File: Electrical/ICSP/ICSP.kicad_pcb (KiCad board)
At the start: 2 copper layers, 8 parts, among them J1 card_edge_6p, J2 card_edge_6p, J3 card_edge_6p, J4 card_edge_6p, J5 card_edge_6p, J6 card_edge_6p

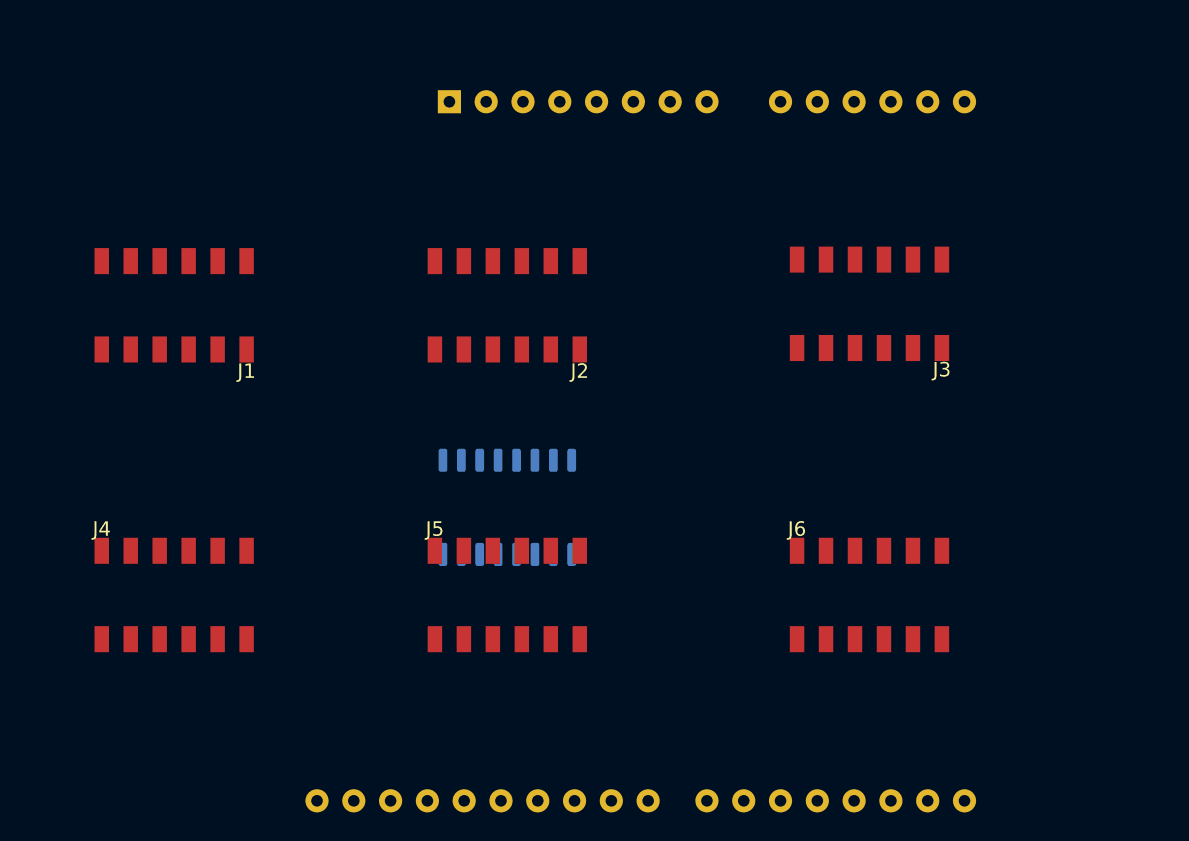
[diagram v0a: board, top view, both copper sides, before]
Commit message: Updated ICSP board.
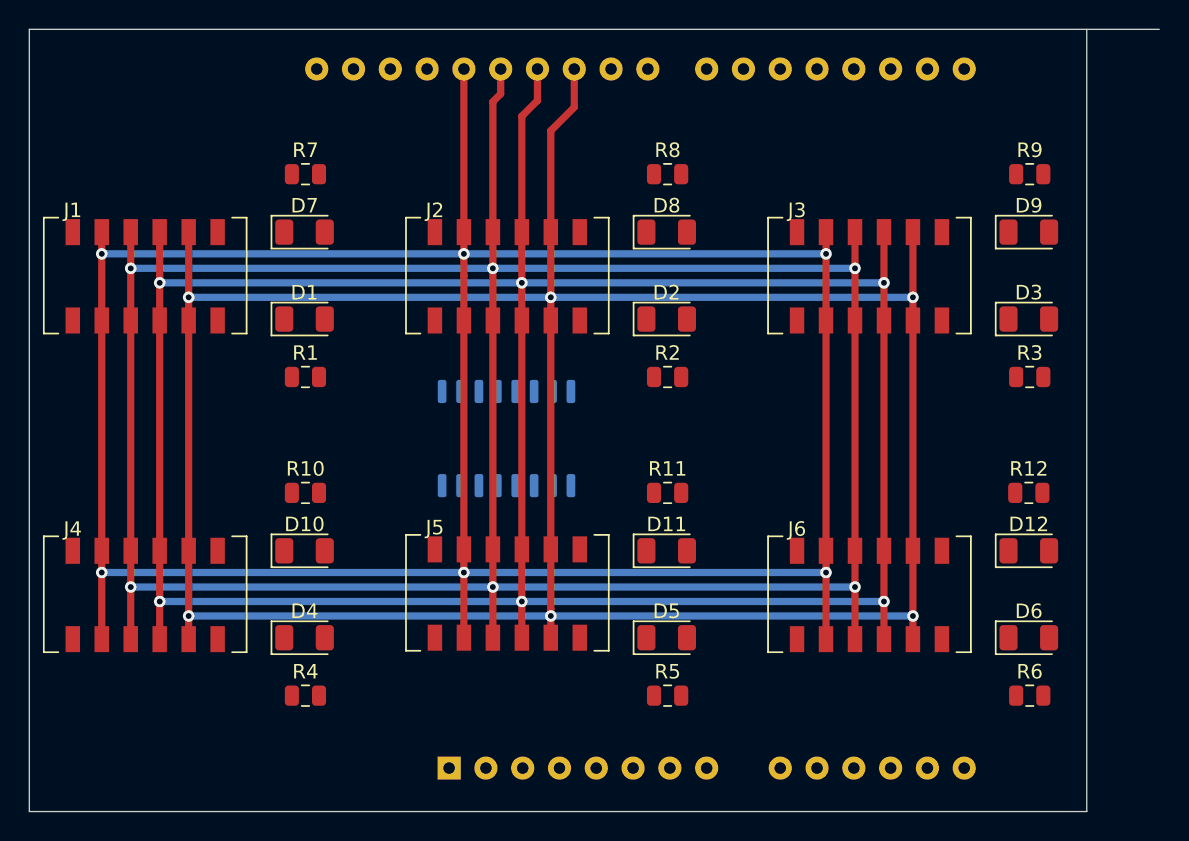
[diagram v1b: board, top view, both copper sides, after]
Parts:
- added D1: rLED, LED_SMD:LED_1206_3216Metric, F.Cu at (104.0, 92.0)
- added D10: gLED, LED_SMD:LED_1206_3216Metric, F.Cu at (104.0, 108.0)
- added D11: gLED, LED_SMD:LED_1206_3216Metric, F.Cu at (129.0, 108.0)
- added D12: gLED, LED_SMD:LED_1206_3216Metric, F.Cu at (154.0, 108.0)
- added D2: rLED, LED_SMD:LED_1206_3216Metric, F.Cu at (129.0, 92.0)
- added D3: rLED, LED_SMD:LED_1206_3216Metric, F.Cu at (154.0, 92.0)
- added D4: rLED, LED_SMD:LED_1206_3216Metric, F.Cu at (104.0, 114.0)
- added D5: rLED, LED_SMD:LED_1206_3216Metric, F.Cu at (129.0, 114.0)
- added D6: rLED, LED_SMD:LED_1206_3216Metric, F.Cu at (154.0, 114.0)
- added D7: gLED, LED_SMD:LED_1206_3216Metric, F.Cu at (104.0, 86.0)
- added D8: gLED, LED_SMD:LED_1206_3216Metric, F.Cu at (129.0, 86.0)
- added D9: gLED, LED_SMD:LED_1206_3216Metric, F.Cu at (154.0, 86.0)
- added R1: R_US, Resistor_SMD:R_0805_2012Metric, F.Cu at (104.1, 96.0)
- added R10: R_US, Resistor_SMD:R_0805_2012Metric, F.Cu at (104.1, 104.0)
- added R11: R_US, Resistor_SMD:R_0805_2012Metric, F.Cu at (129.1, 104.0)
- added R12: R_US, Resistor_SMD:R_0805_2012Metric, F.Cu at (154.0, 104.0)
- added R2: R_US, Resistor_SMD:R_0805_2012Metric, F.Cu at (129.1, 96.0)
- added R3: R_US, Resistor_SMD:R_0805_2012Metric, F.Cu at (154.1, 96.0)
- added R4: R_US, Resistor_SMD:R_0805_2012Metric, F.Cu at (104.1, 118.0)
- added R5: R_US, Resistor_SMD:R_0805_2012Metric, F.Cu at (129.1, 118.0)
- added R6: R_US, Resistor_SMD:R_0805_2012Metric, F.Cu at (154.1, 118.0)
- added R7: R_US, Resistor_SMD:R_0805_2012Metric, F.Cu at (104.1, 82.0)
- added R8: R_US, Resistor_SMD:R_0805_2012Metric, F.Cu at (129.1, 82.0)
- added R9: R_US, Resistor_SMD:R_0805_2012Metric, F.Cu at (154.1, 82.0)
- A1: moved to B.Cu
- moved A1 46.0 mm to (114.0, 123.0)
- moved J1 14.5 mm to (88.0, 86.0), turned to 0 degrees
- moved J2 12.9 mm to (113.0, 86.0), turned to 0 degrees
- moved J3 12.8 mm to (138.0, 86.0), turned to 0 degrees
- moved e1 4.75 mm to (117.9, 100.2), turned to 270 degrees
- moved J4 2.00 mm to (88.0, 108.0)
- moved J5 0.10 mm to (113.0, 107.9)
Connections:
- J1 pad 1: /MISO -> +5V
- J1 pad 2: /Vcc -> /SCK
- J1 pad 3: /SCK -> /MISO
- J1 pad 6: Net-(J1-Pad6) -> /ULN16
- J2 pad 1: Net-(J2-Pad1) -> +5V
- J2 pad 2: Net-(J2-Pad2) -> /SCK
- J2 pad 3: Net-(J2-Pad3) -> /MISO
- J2 pad 4: Net-(J2-Pad4) -> /MOSI
- J2 pad 5: Net-(J2-Pad5) -> /RST
- J2 pad 6: Net-(J2-Pad6) -> /ULN15
- J3 pad 1: Net-(J3-Pad1) -> +5V
- J3 pad 2: Net-(J3-Pad2) -> /SCK
- J3 pad 3: Net-(J3-Pad3) -> /MISO
- J3 pad 4: Net-(J3-Pad4) -> /MOSI
- J3 pad 5: Net-(J3-Pad5) -> /RST
- J3 pad 6: Net-(J3-Pad6) -> /ULN14
- J4 pad 1: Net-(J4-Pad1) -> +5V
- J4 pad 2: Net-(J4-Pad2) -> /SCK
- J4 pad 3: Net-(J4-Pad3) -> /MISO
- J4 pad 4: Net-(J4-Pad4) -> /MOSI
- J4 pad 5: Net-(J4-Pad5) -> /RST
- J4 pad 6: Net-(J4-Pad6) -> /ULN13
- J5 pad 1: Net-(J5-Pad1) -> +5V
- J5 pad 2: Net-(J5-Pad2) -> /SCK
- J5 pad 3: Net-(J5-Pad3) -> /MISO
- J5 pad 4: Net-(J5-Pad4) -> /MOSI
- J5 pad 5: Net-(J5-Pad5) -> /RST
- J5 pad 6: Net-(J5-Pad6) -> /ULN12
- J6 pad 1: Net-(J6-Pad1) -> +5V
- J6 pad 2: Net-(J6-Pad2) -> /SCK
- J6 pad 3: Net-(J6-Pad3) -> /MISO
- J6 pad 4: Net-(J6-Pad4) -> /MOSI
- J6 pad 5: Net-(J6-Pad5) -> /RST
- J6 pad 6: Net-(J6-Pad6) -> /ULN11
- e1 pad 1: Net-(e1-Pad1) -> Net-(A1-Pad23)
- e1 pad 11: Net-(e1-Pad11) -> /ULN11
- e1 pad 12: Net-(e1-Pad12) -> /ULN12
- e1 pad 13: Net-(e1-Pad13) -> /ULN13
- e1 pad 14: Net-(e1-Pad14) -> /ULN14
- e1 pad 15: Net-(e1-Pad15) -> /ULN15
- e1 pad 16: Net-(e1-Pad16) -> /ULN16
- e1 pad 2: Net-(e1-Pad2) -> Net-(A1-Pad22)
- e1 pad 3: Net-(e1-Pad3) -> Net-(A1-Pad21)
- e1 pad 4: Net-(e1-Pad4) -> Net-(A1-Pad20)
- e1 pad 5: Net-(e1-Pad5) -> Net-(A1-Pad19)
- e1 pad 6: Net-(e1-Pad6) -> Net-(A1-Pad18)
- e1 pad 9: Net-(e1-Pad9) -> +5V
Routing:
- net /RST: track 0.00 -> 196.1 mm, vias 0 -> 6
- net /MOSI: track 0.00 -> 195.9 mm, vias 0 -> 6
- net /MISO: track 0.00 -> 195.7 mm, vias 0 -> 6
- net /SCK: track 0.00 -> 195.5 mm, vias 0 -> 6
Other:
- board outline added: 78 x 54 mm

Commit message: Finalized initial ICSP board layout.
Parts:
- R1, R10, R11, R12, R2, R3, R4, R5, R6, R7, R8, R9: moved to B.Cu
- moved R12 4.72 mm to (156.5, 108.0)
- moved R1 4.68 mm to (106.5, 92.0)
- moved R10 4.68 mm to (106.5, 108.0)
- moved R11 4.68 mm to (131.5, 108.0)
- moved R2 4.68 mm to (131.5, 92.0)
- moved R4 4.68 mm to (106.5, 114.0)
- moved R5 4.68 mm to (131.5, 114.0)
- moved R6 4.68 mm to (156.5, 114.0)
- moved R7 4.68 mm to (106.5, 86.0)
- moved R8 4.68 mm to (131.5, 86.0)
- moved R9 4.68 mm to (156.5, 86.0)
- moved R3 4.44 mm to (156.0, 92.0)
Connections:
- R7 pad 1: Net-(A1-Pad9) -> Net-(A1-Pad17)
- R8 pad 1: Net-(A1-Pad10) -> Net-(A1-Pad16)
- R9 pad 1: Net-(A1-Pad11) -> Net-(A1-Pad15)
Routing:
- net +5V: track 0.00 -> 283.2 mm, vias 0 -> 8
- net Net-(A1-Pad12): track 0.00 -> 56.6 mm, vias 0 -> 3
- net /ULN14: track 0.00 -> 49.7 mm, vias 0 -> 1
- net Net-(A1-Pad17): track 0.00 -> 48.5 mm
- net GND: track 0.00 -> 47.4 mm, vias 0 -> 8
- net /ULN11: track 0.00 -> 44.8 mm, vias 0 -> 1
- net Net-(A1-Pad22): track 0.00 -> 42.7 mm, vias 0 -> 2
- net Net-(A1-Pad21): track 0.00 -> 42.7 mm, vias 0 -> 2
- net Net-(A1-Pad23): track 0.00 -> 40.2 mm, vias 0 -> 2
- net Net-(A1-Pad19): track 0.00 -> 39.9 mm, vias 0 -> 1
- net Net-(A1-Pad18): track 0.00 -> 39.4 mm, vias 0 -> 1
- net /ULN13: track 0.00 -> 36.6 mm, vias 0 -> 1
- net Net-(A1-Pad20): track 0.00 -> 35.1 mm, vias 0 -> 2
- net /ULN15: track 0.00 -> 33.3 mm, vias 0 -> 1
- net /ULN16: track 0.00 -> 32.1 mm, vias 0 -> 1
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- added copper zone on B.Cu, net GND
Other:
- board size 78 x 54 mm -> 74.5 x 54 mm
- rule via_min_size: 0.4 -> 0.3

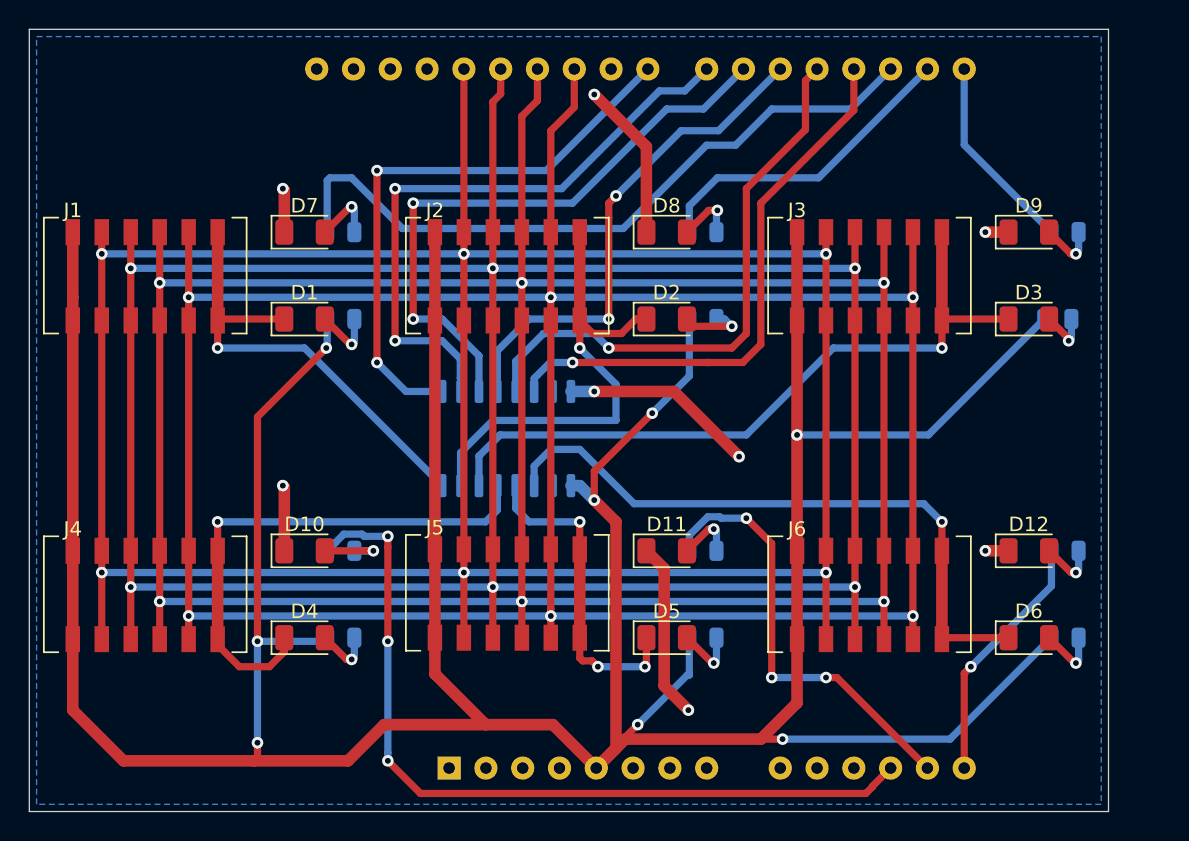
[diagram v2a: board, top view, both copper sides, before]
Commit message: Cleaned up folders for USB and ICSP boards.
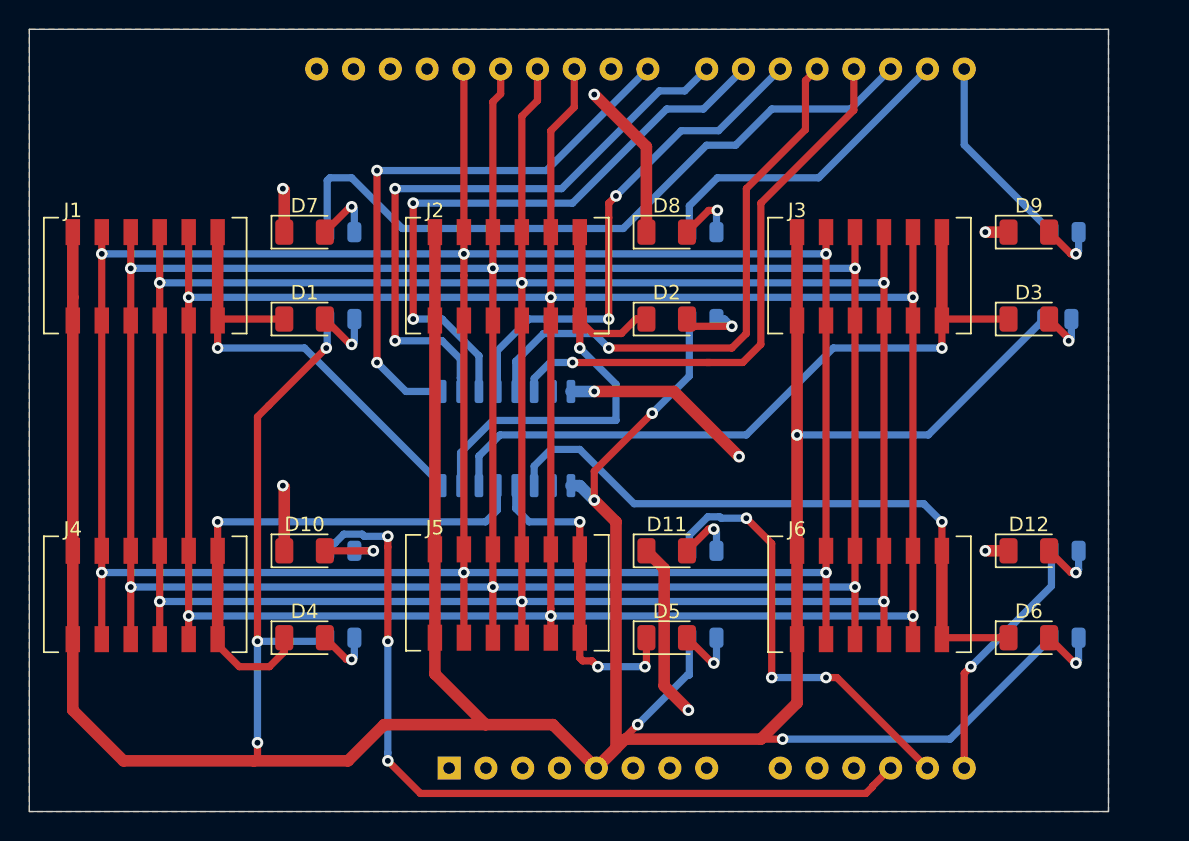
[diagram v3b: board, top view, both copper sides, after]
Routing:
- added copper zone on F.Cu, net GND
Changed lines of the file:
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@@
   )
   (setup
-    (last_trace_width 0.5)
+    (last_trace_width 0.25)
     (user_trace_width 0.5)
     (user_trace_width 0.8)
     (trace_clearance 0.2)
-    (zone_clearance 0.508)
+    (zone_clearance 0.2)
     (zone_45_only no)
     (trace_min 0.2)
@@
   (segment (start 157.25 109.5) (end 156.9 109.5) (width 0.5) (layer F.Cu) (net 50))
   (zone (net 29) (net_name GND) (layer B.Cu) (hatch edge 0.508)
-    (connect_pads (clearance 0.508))
-    (min_thickness 0.254)
+    (connect_pads (clearance 0.2))
+    (min_thickness 0.2)
     (fill yes (arc_segments 32) (thermal_gap 0.508) (thermal_bridge_width 0.508))
     (polygon
       (pts
-        (xy 85.5 72.5) (xy 159 72.5) (xy 159 125.5) (xy 85.5 125.5)
+        (xy 85 72) (xy 159.5 72) (xy 159.5 126) (xy 85 126)
       )
     )
+  )
+  (zone (net 29) (net_name GND) (layer F.Cu) (hatch edge 0.508)
+    (connect_pads (clearance 0.2))
+    (min_thickness 0.2)
+    (fill yes (arc_segments 32) (thermal_gap 0.508) (thermal_bridge_width 0.508))
+    (polygon
+      (pts
+        (xy 85 72) (xy 159.5 72) (xy 159.5 126) (xy 85 126)
+      )
+    )

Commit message: Began exstablishing files for Mechanical design.
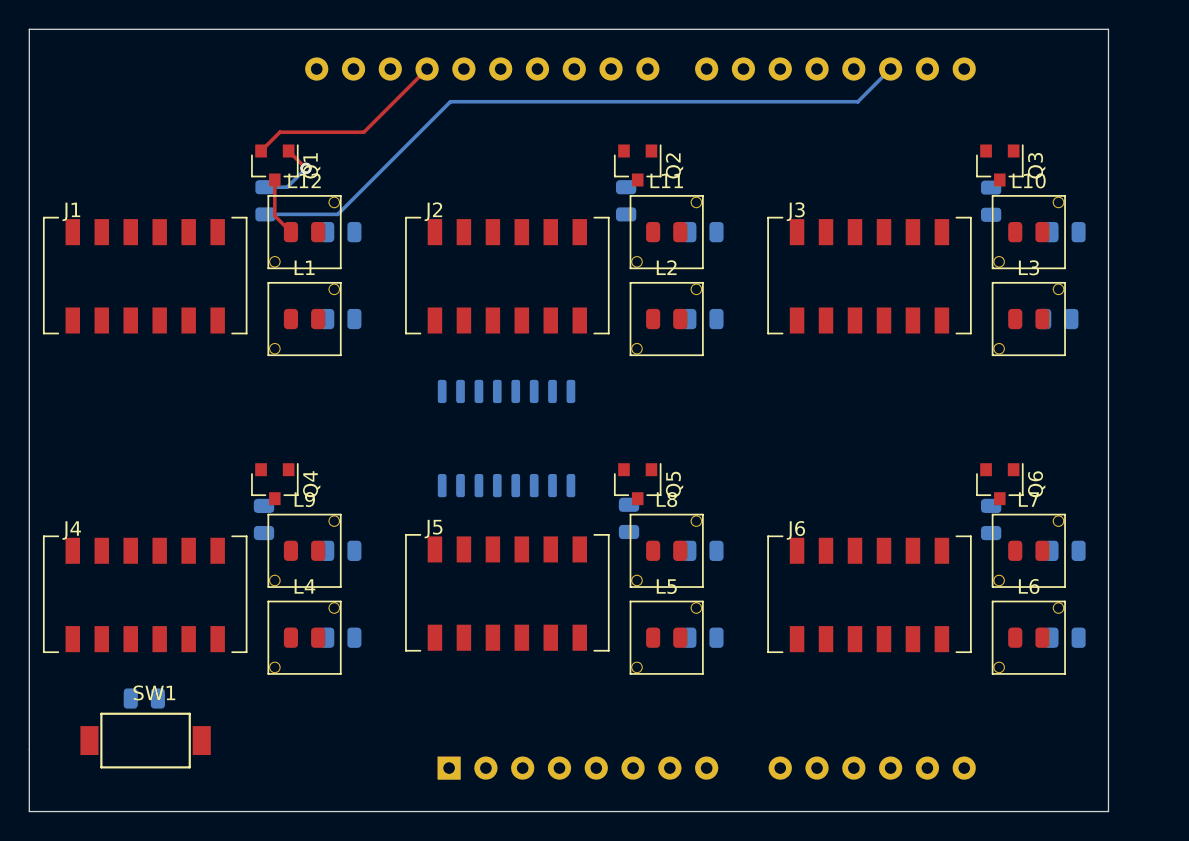
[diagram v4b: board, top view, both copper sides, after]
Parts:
- added Q1: BC850, Package_TO_SOT_SMD:SOT-23, F.Cu at (102.0, 81.4)
- added Q2: BC850, Package_TO_SOT_SMD:SOT-23, F.Cu at (127.0, 81.4)
- added Q3: BC850, Package_TO_SOT_SMD:SOT-23, F.Cu at (152.0, 81.4)
- added Q4: BC850, Package_TO_SOT_SMD:SOT-23, F.Cu at (102.0, 103.4)
- added Q5: BC850, Package_TO_SOT_SMD:SOT-23, F.Cu at (127.0, 103.4)
- added Q6: BC850, Package_TO_SOT_SMD:SOT-23, F.Cu at (152.0, 103.4)
- added R13: R_US, Resistor_SMD:R_0805_2012Metric, B.Cu at (151.4, 105.8)
- added R14: R_US, Resistor_SMD:R_0805_2012Metric, B.Cu at (126.2, 83.8)
- added R15: R_US, Resistor_SMD:R_0805_2012Metric, B.Cu at (101.2, 105.8)
- added R16: R_US, Resistor_SMD:R_0805_2012Metric, B.Cu at (101.3, 83.8)
- added R17: R_US, Resistor_SMD:R_0805_2012Metric, B.Cu at (151.4, 83.9)
- added R18: R_US, Resistor_SMD:R_0805_2012Metric, B.Cu at (126.4, 105.8)
- added R19: R_US, Resistor_SMD:R_0805_2012Metric, B.Cu at (92.9, 118.2)
- added SW1: SW_Push, hodgkin:PTS636-G-2.5-NoGND, F.Cu at (96.9, 121.1)
- L1: renamed from D1; footprint LED_SMD:LED_1206_3216Metric -> hodgkin:LED_0805_LightPipe
- L10: renamed from D9; footprint LED_SMD:LED_1206_3216Metric -> hodgkin:LED_0805_LightPipe
- L11: renamed from D8; footprint LED_SMD:LED_1206_3216Metric -> hodgkin:LED_0805_LightPipe
- L12: renamed from D7; footprint LED_SMD:LED_1206_3216Metric -> hodgkin:LED_0805_LightPipe
- L2: renamed from D2; footprint LED_SMD:LED_1206_3216Metric -> hodgkin:LED_0805_LightPipe
- L3: renamed from D3; footprint LED_SMD:LED_1206_3216Metric -> hodgkin:LED_0805_LightPipe
- L4: renamed from D4; footprint LED_SMD:LED_1206_3216Metric -> hodgkin:LED_0805_LightPipe
- L5: renamed from D5; footprint LED_SMD:LED_1206_3216Metric -> hodgkin:LED_0805_LightPipe
- L6: renamed from D6; footprint LED_SMD:LED_1206_3216Metric -> hodgkin:LED_0805_LightPipe
- L7: renamed from D12; footprint LED_SMD:LED_1206_3216Metric -> hodgkin:LED_0805_LightPipe
- L8: renamed from D11; footprint LED_SMD:LED_1206_3216Metric -> hodgkin:LED_0805_LightPipe
- L9: renamed from D10; footprint LED_SMD:LED_1206_3216Metric -> hodgkin:LED_0805_LightPipe
- renumbered R9 to R10, R8 to R11, R7 to R12, R12 to R7, R11 to R8, R10 to R9
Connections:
- A1 pad 3: Net-(A1-Pad3) -> /SW1
- L10 pad 1: GND -> /G3
- L11 pad 1: GND -> /G2
- L12 pad 1: GND -> /G1
- L7 pad 1: GND -> /G6
- L8 pad 1: GND -> /G5
- L9 pad 1: GND -> /G4
- R10 pad 1: Net-(A1-Pad15) -> +5V
- R11 pad 1: Net-(A1-Pad16) -> +5V
- R12 pad 1: Net-(A1-Pad17) -> +5V
- R7 pad 1: Net-(A1-Pad14) -> +5V
- R8 pad 1: Net-(A1-Pad13) -> +5V
- R9 pad 1: Net-(A1-Pad12) -> +5V
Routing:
- net +5V: track 283.2 -> 0.00 mm, vias 8 -> 0
- net /RST: track 196.1 -> 0.00 mm, vias 6 -> 0
- net /MOSI: track 195.9 -> 0.00 mm, vias 6 -> 0
- net /MISO: track 195.7 -> 0.00 mm, vias 6 -> 0
- net /SCK: track 195.5 -> 0.00 mm, vias 6 -> 0
- net Net-(A1-Pad12): track 56.6 -> 0.00 mm, vias 3 -> 0
- net /ULN14: track 49.7 -> 0.00 mm, vias 1 -> 0
- net /ULN11: track 44.8 -> 0.00 mm, vias 1 -> 0
- net Net-(A1-Pad22): track 42.7 -> 0.00 mm, vias 2 -> 0
- net Net-(A1-Pad21): track 42.7 -> 0.00 mm, vias 2 -> 0
- net Net-(A1-Pad23): track 40.2 -> 0.00 mm, vias 2 -> 0
- net Net-(A1-Pad19): track 39.9 -> 0.00 mm, vias 1 -> 0
- net Net-(A1-Pad18): track 39.4 -> 0.00 mm, vias 1 -> 0
- net /ULN13: track 36.6 -> 0.00 mm, vias 1 -> 0
- net Net-(A1-Pad20): track 35.1 -> 0.00 mm, vias 2 -> 0
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- removed copper zone on B.Cu, net GND
- removed copper zone on F.Cu, net GND
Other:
- outline, holes or cut-outs redrawn
